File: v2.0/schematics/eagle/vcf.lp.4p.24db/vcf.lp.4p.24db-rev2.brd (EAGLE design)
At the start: 98.7 x 71.1 mm, 83 parts, among them IC1 TL082P, IC2 TL084P, IC3 TL084P, IC4 LM13700N, IC5 LM13700N, J1 IN, J2 OUT, T1 2N3904, T2 2N3904, T3 2N3906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

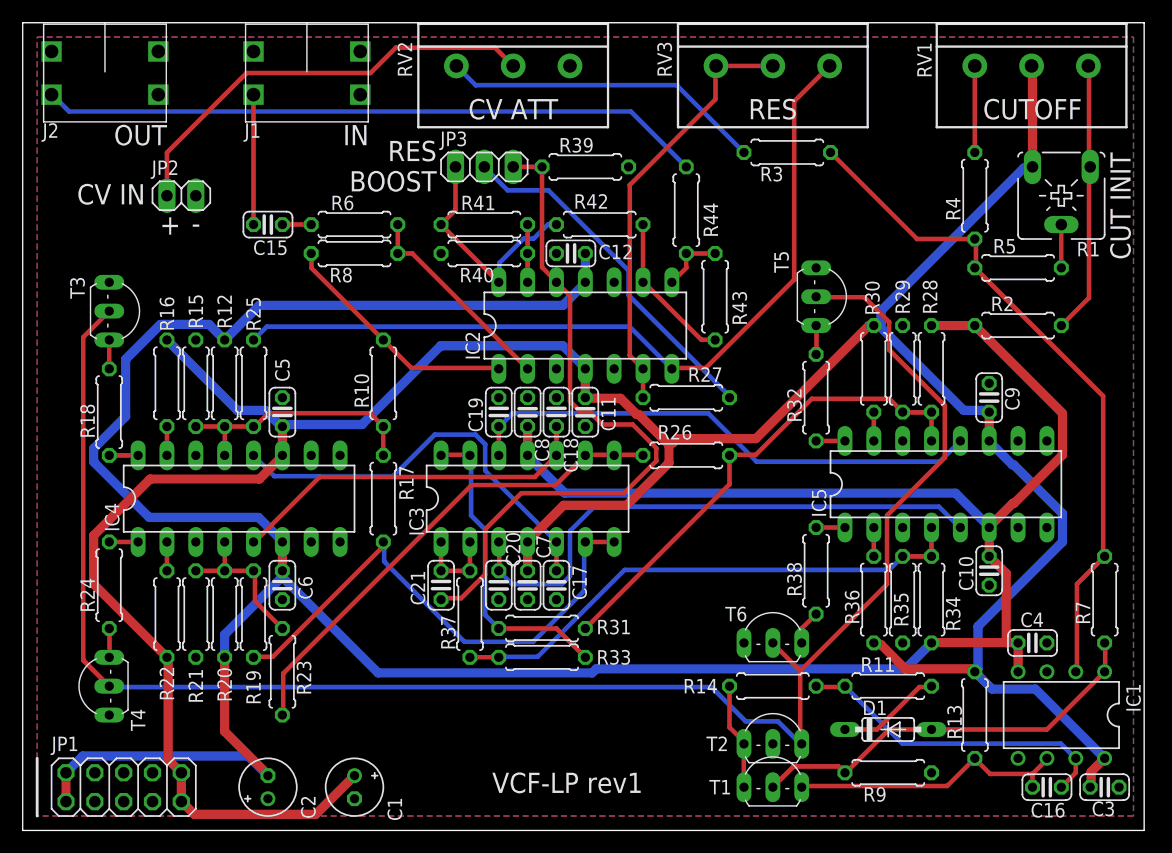
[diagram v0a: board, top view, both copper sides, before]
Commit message: Corrected R-VAR pin 2 & 3 mapping for VCFLP and LFOVCA
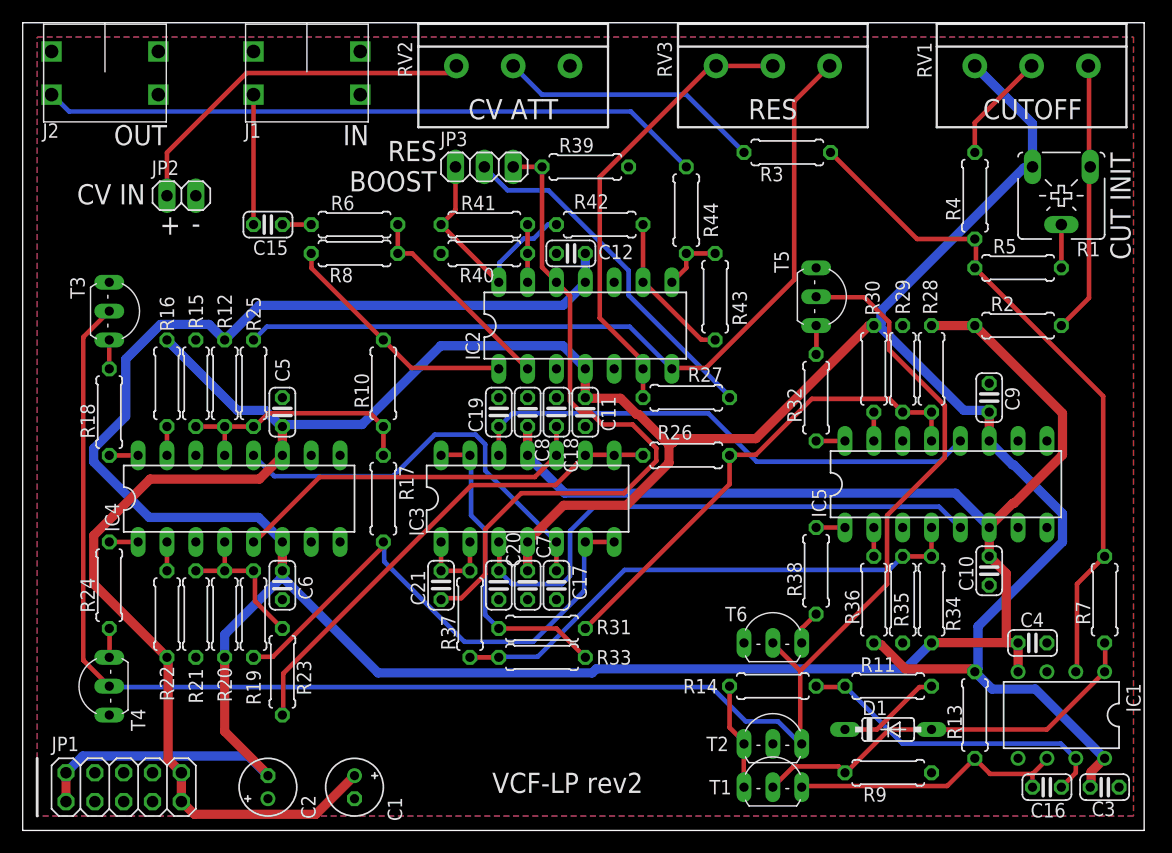
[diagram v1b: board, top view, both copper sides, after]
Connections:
- net +12V: now also RV1.3; no longer RV1.2
- net N$13: now also RV2.2; no longer RV2.3
- net N$2: now also RV1.2; no longer RV1.3
- net N$3: now also RV2.3; no longer RV2.2
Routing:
- net N$3: track 38.8 -> 32.4 mm
- net N$13: track 28.5 -> 23.5 mm
- net N$50: track 37.8 -> 40.3 mm
- net +12V: track 261.7 -> 263.8 mm
- net N$2: track 7.62 -> 9.69 mm
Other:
- board text added: "VCF-LP rev2"
- board text removed: "R-VAR PIN MAP IS WRONG! Pins 2 and 3 are swapped!!!"
- board text removed: "VCF-LP rev1"
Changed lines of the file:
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@@
 <layer number="25" name="tNames" color="7" fill="1" visible="yes" active="yes"/>
 <layer number="26" name="bNames" color="7" fill="1" visible="yes" active="yes"/>
-<layer number="27" name="tValues" color="7" fill="1" visible="yes" active="yes"/>
+<layer number="27" name="tValues" color="7" fill="1" visible="no" active="yes"/>
 <layer number="28" name="bValues" color="7" fill="1" visible="no" active="yes"/>
 <layer number="29" name="tStop" color="7" fill="3" visible="no" active="yes"/>
@@
 <wire x1="0" y1="71.11" x2="0" y2="0" width="0" layer="20"/>
 <wire x1="1.27" y1="1.27" x2="1.27" y2="6.35" width="0.254" layer="21"/>
-<text x="54.61" y="5.08" size="1.778" layer="25" rot="R180">VCF-LP rev1</text>
+<text x="54.61" y="5.08" size="1.778" layer="25" rot="R180">VCF-LP rev2</text>
 <text x="88.9" y="63.5" size="1.778" layer="25" align="center">CUTOFF</text>
 <text x="43.18" y="63.5" size="1.778" layer="25" align="center">CV ATT</text>
@@
 <text x="12.065" y="52.451" size="1.778" layer="25">+</text>
 <text x="14.859" y="52.578" size="1.778" layer="25">-</text>
-<text x="58.42" y="72.39" size="1.778" layer="51">R-VAR PIN MAP
-IS WRONG!
-Pins 2 and 3
-are swapped!!!</text>
-<text x="35.56" y="72.39" size="1.778" layer="51">R-VAR PIN MAP
-IS WRONG!
-Pins 2 and 3
-are swapped!!!</text>
-<text x="81.28" y="72.39" size="1.778" layer="51">R-VAR PIN MAP
-IS WRONG!
-Pins 2 and 3
-are swapped!!!</text>
 </plain>
 <attributes>
@@
 <contactref element="JP1" pad="9"/>
 <contactref element="JP1" pad="10"/>
-<contactref element="RV1" pad="2"/>
+<contactref element="RV1" pad="3"/>
 <contactref element="R1" pad="E"/>
 <contactref element="R13" pad="2"/>
@@
 <wire x1="57.2516" y1="34.1376" x2="57.6072" y2="34.4932" width="0.8128" layer="1"/>
 <wire x1="57.2516" y1="34.1376" x2="56.896" y2="33.9598" width="0.8128" layer="1"/>
-<wire x1="88.82" y1="67.31" x2="88.9" y2="67.23" width="0.8128" layer="1"/>
-<wire x1="88.9" y1="67.23" x2="88.9" y2="58.42" width="0.8128" layer="1"/>
 <wire x1="94.0562" y1="5.1562" x2="94.0562" y2="3.8862" width="0.8128" layer="1"/>
 <wire x1="94.0562" y1="3.8862" x2="93.98" y2="3.81" width="0.8128" layer="1"/>
@@
 <wire x1="85.344" y1="12.446" x2="89.154" y2="12.446" width="0.8128" layer="16"/>
 <wire x1="89.154" y1="12.446" x2="95.25" y2="6.35" width="0.8128" layer="16"/>
+<wire x1="88.9" y1="58.42" x2="88.9" y2="62.23" width="0.8128" layer="16"/>
+<wire x1="88.9" y1="62.23" x2="83.82" y2="67.31" width="0.8128" layer="16"/>
 </signal>
 <signal name="-12V" class="1">
@@
 </signal>
 <signal name="N$2">
-<contactref element="RV1" pad="3"/>
+<contactref element="RV1" pad="2"/>
 <contactref element="R4" pad="1"/>
-<wire x1="83.82" y1="67.31" x2="83.82" y2="59.69" width="0.4064" layer="1"/>
+<wire x1="88.82" y1="67.31" x2="83.82" y2="62.31" width="0.4064" layer="1"/>
+<wire x1="83.82" y1="62.31" x2="83.82" y2="59.69" width="0.4064" layer="1"/>
 </signal>
 <signal name="N$5">
@@
 <signal name="N$50">
 <contactref element="R27" pad="1"/>
+<contactref element="RV3" pad="2"/>
 <contactref element="RV3" pad="3"/>
-<contactref element="RV3" pad="2"/>
 <contactref element="IC2" pad="6"/>
-<wire x1="61.04" y1="67.31" x2="60.9854" y2="67.2554" width="0.4064" layer="1"/>
-<wire x1="60.9854" y1="67.2554" x2="60.9854" y2="64.3636" width="0.4064" layer="1"/>
-<wire x1="60.9854" y1="64.3636" x2="53.4416" y2="56.8198" width="0.4064" layer="1"/>
-<wire x1="53.4416" y1="56.8198" x2="53.4416" y2="41.8084" width="0.4064" layer="1"/>
-<wire x1="53.4416" y1="41.8084" x2="54.61" y2="40.64" width="0.4064" layer="1"/>
-<wire x1="54.61" y1="40.64" x2="54.61" y2="38.1" width="0.4064" layer="1"/>
+<wire x1="61.04" y1="67.31" x2="60.57761875" y2="67.31" width="0.4064" layer="1"/>
+<wire x1="60.57761875" y1="67.31" x2="50.8" y2="57.53238125" width="0.4064" layer="1"/>
+<wire x1="50.8" y1="57.53238125" x2="50.8" y2="45.1104" width="0.4064" layer="1"/>
+<wire x1="50.8" y1="45.1104" x2="54.61" y2="41.3004" width="0.4064" layer="1"/>
+<wire x1="54.61" y1="41.3004" x2="54.61" y2="40.64" width="0.4064" layer="1"/>
 <wire x1="61.04" y1="67.31" x2="66.04" y2="67.31" width="0.4064" layer="1"/>
+<wire x1="54.61" y1="40.64" x2="54.61" y2="39.9796" width="0.4064" layer="1"/>
+<wire x1="54.61" y1="39.9796" x2="54.61" y2="38.1" width="0.4064" layer="1"/>
 </signal>
 <signal name="N$47">
@@
 <signal name="N$3">
 <contactref element="JP2" pad="1"/>
-<contactref element="RV2" pad="2"/>
-<wire x1="43.18" y1="67.31" x2="41.5798" y2="68.9102" width="0.4064" layer="1"/>
-<wire x1="41.5798" y1="68.9102" x2="32.8502" y2="68.9102" width="0.4064" layer="1"/>
-<wire x1="32.8502" y1="68.9102" x2="30.62" y2="66.68" width="0.4064" layer="1"/>
-<wire x1="30.62" y1="66.68" x2="19.701559375" y2="66.68" width="0.4064" layer="1"/>
+<contactref element="RV2" pad="3"/>
+<wire x1="38.18" y1="67.31" x2="37.55" y2="66.68" width="0.4064" layer="1"/>
+<wire x1="37.55" y1="66.68" x2="19.701559375" y2="66.68" width="0.4064" layer="1"/>
 <wire x1="19.701559375" y1="66.68" x2="12.7" y2="59.678440625" width="0.4064" layer="1"/>
 <wire x1="12.7" y1="59.678440625" x2="12.7" y2="56.642" width="0.4064" layer="1"/>
@@
 </signal>
 <signal name="N$13">
-<contactref element="RV2" pad="3"/>
+<contactref element="RV2" pad="2"/>
 <contactref element="R3" pad="1"/>
-<wire x1="38.18" y1="67.31" x2="39.8818" y2="65.6082" width="0.4064" layer="16"/>
-<wire x1="39.8818" y1="65.6082" x2="57.5818" y2="65.6082" width="0.4064" layer="16"/>
-<wire x1="57.5818" y1="65.6082" x2="63.5" y2="59.69" width="0.4064" layer="16"/>
+<wire x1="63.5" y1="59.69" x2="58.404859375" y2="64.785140625" width="0.4064" layer="16"/>
+<wire x1="58.404859375" y1="64.785140625" x2="45.704859375" y2="64.785140625" width="0.4064" layer="16"/>
+<wire x1="45.704859375" y1="64.785140625" x2="43.18" y2="67.31" width="0.4064" layer="16"/>
 </signal>
 </signals>

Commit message: VCFLP - updated rev3 with zenner clipping
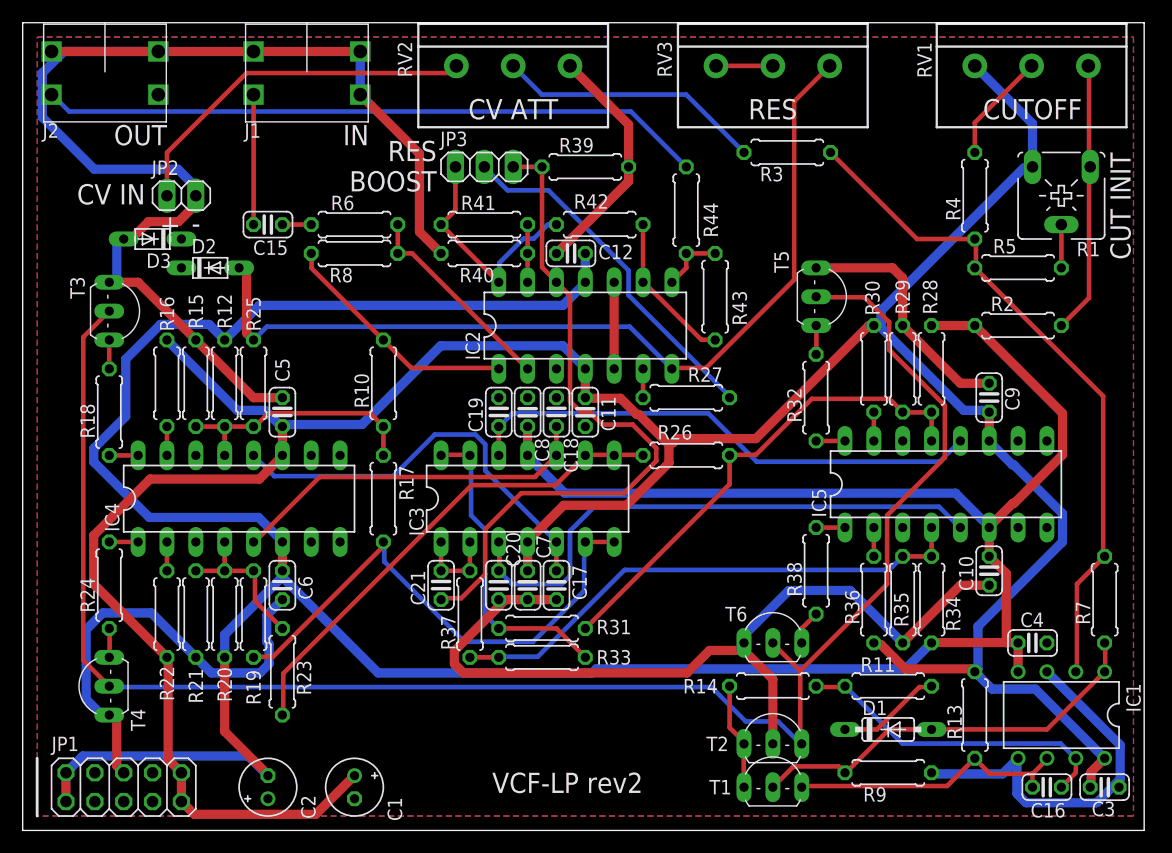
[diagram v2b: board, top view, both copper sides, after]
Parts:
- added D2, D3: 1N5232B, _common:DO34-5
- R25: value 27K -> 100K
- R27: value 10K -> 68K
- RV3: value 10K (B) -> 250K (B)
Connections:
- new net N$35: D2.C, D3.C
- net 0V: now also D3.A
- net N$47: now also D2.A
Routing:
- net 0V: track 0.00 -> 314.6 mm
- net N$50: track 40.3 -> 8.00 mm
- net N$47: track 73.0 -> 80.2 mm
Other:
- board text added: "The board needs a serious rework on the layout and routing."

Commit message: VFCLP: Changed RES++ switch into 2/4 Pole select switch
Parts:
- added R45: 20K, resistor:0207/7
- JP3: value RES BOOST -> 2 POLE / 4 POLE
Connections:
- removed net N$40: JP3.2, R27.2
- new net N$36: C21.2, JP3.2
- new net N$37: JP3.1, R45.2
- net N$25: now also R45.1
- net N$39: no longer JP3.3
- net N$43: now also R27.2; no longer JP3.1
- net N$65: now also JP3.3; no longer C21.2
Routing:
- net N$40: track 31.4 -> 0.00 mm
- net N$65: track 7.62 -> 2.54 mm
- net N$43: track 20.9 -> 17.1 mm
- net N$39: track 60.9 -> 58.4 mm
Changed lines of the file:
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@@
 <attribute name="VALUE" x="54.102" y="49.403" size="1.27" layer="27" ratio="10"/>
 </element>
-<element name="JP3" library="pinhead" library_urn="urn:adsk.eagle:library:325" package="1X03" package3d_urn="urn:adsk.eagle:package:22458/2" value="RES BOOST" x="40.64" y="58.42" smashed="yes">
+<element name="JP3" library="pinhead" library_urn="urn:adsk.eagle:library:325" package="1X03" package3d_urn="urn:adsk.eagle:package:22458/2" value="2 POLE / 4 POLE" x="40.64" y="58.42" smashed="yes">
 <attribute name="NAME" x="36.7538" y="60.2488" size="1.27" layer="25" ratio="10"/>
 <attribute name="POPULARITY" value="92" x="40.64" y="58.42" size="1.778" layer="27" display="off"/>
@@
 <attribute name="NAME" x="13.081" y="50.8" size="1.27" layer="25" ratio="10" rot="R180"/>
 <attribute name="VALUE" x="13.081" y="54.61" size="1.27" layer="27" ratio="10" rot="R180"/>
+</element>
+<element name="R45" library="resistor" package="0207/7" value="20K" x="34.29" y="13.97" smashed="yes" rot="R90">
+<attribute name="NAME" x="32.893" y="11.43" size="1.27" layer="25" ratio="10" rot="R90"/>
+<attribute name="VALUE" x="34.8488" y="11.684" size="1.27" layer="27" ratio="10" rot="R90"/>
 </element>
 </elements>
@@
 <wire x1="39.52103125" y1="30.4038" x2="22.9362" y2="13.81896875" width="0.4064" layer="1"/>
 <wire x1="22.9362" y1="13.81896875" x2="22.9362" y2="10.2362" width="0.4064" layer="1"/>
+<contactref element="R45" pad="1"/>
+<wire x1="34.29" y1="10.16" x2="22.86" y2="10.16" width="0" layer="19" extent="1-1"/>
 </signal>
 <signal name="N$26">
@@
 <signal name="N$43">
 <contactref element="R41" pad="2"/>
-<contactref element="JP3" pad="1"/>
 <contactref element="R42" pad="1"/>
 <contactref element="IC2" pad="14"/>
@@
 <wire x1="41.9608" y1="49.96316875" x2="44.09303125" y2="52.0954" width="0.4064" layer="16"/>
 <wire x1="44.09303125" y1="52.0954" x2="44.9834" y2="52.0954" width="0.4064" layer="16"/>
-<wire x1="38.1" y1="58.42" x2="38.1" y2="54.61" width="0.4064" layer="1"/>
 <wire x1="38.1" y1="54.61" x2="36.83" y2="53.34" width="0.4064" layer="1"/>
+<contactref element="R27" pad="2"/>
+<wire x1="46.99" y1="53.34" x2="62.23" y2="38.1" width="0" layer="19" extent="1-1"/>
 </signal>
 <signal name="N$44">
@@
 <contactref element="IC3" pad="1"/>
 <contactref element="IC3" pad="2"/>
-<contactref element="C21" pad="2"/>
 <wire x1="39.37" y1="25.4" x2="39.37" y2="22.86" width="0.4064" layer="1"/>
-<wire x1="39.37" y1="22.86" x2="36.83" y2="22.86" width="0.4064" layer="1"/>
-<wire x1="36.83" y1="25.4" x2="36.83" y2="22.86" width="0.4064" layer="1"/>
+<contactref element="JP3" pad="3"/>
+<wire x1="39.37" y1="25.4" x2="43.18" y2="58.42" width="0" layer="19" extent="1-1"/>
+<wire x1="36.83" y1="25.4" x2="39.37" y2="25.4" width="0" layer="19" extent="1-1"/>
 </signal>
 <signal name="N$39">
 <contactref element="C21" pad="1"/>
 <contactref element="R39" pad="2"/>
-<contactref element="JP3" pad="3"/>
 <contactref element="IC2" pad="12"/>
 <wire x1="51.0286" y1="35.7378" x2="53.6956" y2="35.7378" width="0.4064" layer="1"/>
@@
 <wire x1="46.99" y1="48.3108" x2="45.72" y2="49.5808" width="0.4064" layer="1"/>
 <wire x1="45.72" y1="49.5808" x2="45.72" y2="58.42" width="0.4064" layer="1"/>
-<wire x1="43.18" y1="58.42" x2="45.72" y2="58.42" width="0.4064" layer="1"/>
-</signal>
-<signal name="N$40">
-<contactref element="R27" pad="2"/>
-<contactref element="JP3" pad="2"/>
-<wire x1="53.34" y1="47.117" x2="62.23" y2="38.227" width="0.4064" layer="16"/>
-<wire x1="62.23" y1="38.227" x2="62.23" y2="38.1" width="0.4064" layer="16"/>
-<wire x1="40.64" y1="58.42" x2="40.64" y2="58.40194375" width="0.4064" layer="16"/>
-<wire x1="40.64" y1="58.40194375" x2="42.67934375" y2="56.3626" width="0.4064" layer="16"/>
-<wire x1="42.67934375" y1="56.3626" x2="46.28016875" y2="56.3626" width="0.4064" layer="16"/>
-<wire x1="46.28016875" y1="56.3626" x2="53.34" y2="49.30276875" width="0.4064" layer="16"/>
-<wire x1="53.34" y1="49.30276875" x2="53.34" y2="47.117" width="0.4064" layer="16"/>
 </signal>
 <signal name="N$64">
@@
 <wire x1="13.97" y1="49.53" x2="13.97" y2="52.07" width="0" layer="19" extent="1-1"/>
 </signal>
+<signal name="N$36">
+<contactref element="C21" pad="2"/>
+<contactref element="JP3" pad="2"/>
+<wire x1="36.83" y1="22.86" x2="40.64" y2="58.42" width="0" layer="19" extent="1-1"/>
+</signal>
+<signal name="N$37">
+<contactref element="JP3" pad="1"/>
+<contactref element="R45" pad="2"/>
+<wire x1="34.29" y1="17.78" x2="38.1" y2="58.42" width="0" layer="19" extent="1-1"/>
+</signal>
 </signals>
